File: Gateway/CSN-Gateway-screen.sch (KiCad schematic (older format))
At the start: 17 parts, among them IC2 FT232RL, P1 USB_MINI, P2 CONN_01X12, P4 CONN_OLED_SCREEN, SW1 SW_PUSH, SW2 SW_PUSH

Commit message: new pcb for v1.1 prototype
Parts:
- removed C2: 0.1uF, Capacitors_SMD:C_0805_HandSoldering, symbol C
- removed R20: 4k7, Resistors_SMD:R_0805_HandSoldering, symbol R
- removed R21: 10k, Resistors_SMD:R_0805_HandSoldering, symbol R
- added C1: 100nF, Capacitors_SMD:C_0805_HandSoldering, symbol C
- C19: value 100nF -> 10uF; footprint Capacitors_SMD:C_0805_HandSoldering -> Capacitors_Tantalum_SMD:CP_Tantalum_Case-R_EIA-2012-12_Hand; symbol C -> CP1
- P2: footprint Pin_Headers:Pin_Header_Straight_1x12 -> Connectors:IDC_Header_Straight_12pins
- R16, R22, R23: value 100 -> 1K
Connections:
- net GND: now also C1.1
- net RST: now also IC2.2 (!DTR)
- net VCC: no longer C15.1, C19.1, IC2.20 (VCC), IC2.4 (VCCIO)
- net at IC2.17 (3V3OUT): now also C1.2
- net at P1.1 (VCC): now also C15.1, C19.1, IC2.20 (VCC), IC2.4 (VCCIO)
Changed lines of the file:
@@
 P 5650 4050
 F 0 "R16" V 5730 4050 50  0000 C CNN
-F 1 "100" V 5650 4050 50  0000 C CNN
+F 1 "1K" V 5650 4050 50  0000 C CNN
 F 2 "Resistors_SMD:R_0805_HandSoldering" V 5580 4050 50  0001 C CNN
 F 3 "" H 5650 4050 50  0000 C CNN
@@
 NoConn ~ 7100 2300
 NoConn ~ 7100 2400
-NoConn ~ 5900 1700
-$Comp
-L C C2
-U 1 1 583B6E0E
-P 7450 1800
-F 0 "C2" H 7475 1900 50  0000 L CNN
-F 1 "0.1uF" H 7475 1700 50  0000 L CNN
-F 2 "Capacitors_SMD:C_0805_HandSoldering" H 7488 1650 50  0001 C CNN
-F 3 "" H 7450 1800 50  0000 C CNN
-	1    7450 1800
-	0    1    1    0
-$EndComp
-Text GLabel 7750 1800 2    60   Input ~ 0
+Text GLabel 7300 1800 2    60   Input ~ 0
 RST
 $Comp
@@
 	0    -1   1    0
 $EndComp
-$Comp
-L R R20
-U 1 1 583B4E04
-P 5200 2000
-F 0 "R20" V 5280 2000 50  0000 C CNN
-F 1 "4k7" V 5200 2000 50  0000 C CNN
-F 2 "Resistors_SMD:R_0805_HandSoldering" V 5130 2000 50  0001 C CNN
-F 3 "" H 5200 2000 50  0000 C CNN
-	1    5200 2000
-	1    0    0    -1
-$EndComp
-$Comp
-L R R21
-U 1 1 583B4EB8
-P 5200 2500
-F 0 "R21" V 5280 2500 50  0000 C CNN
-F 1 "10k" V 5200 2500 50  0000 C CNN
-F 2 "Resistors_SMD:R_0805_HandSoldering" V 5130 2500 50  0001 C CNN
-F 3 "" H 5200 2500 50  0000 C CNN
-	1    5200 2500
-	1    0    0    -1
-$EndComp
-$Comp
-L GND #PWR08
-U 1 1 583B546D
-P 5200 2800
-F 0 "#PWR08" H 5200 2550 50  0001 C CNN
-F 1 "GND" H 5200 2650 50  0000 C CNN
-F 2 "" H 5200 2800 50  0000 C CNN
-F 3 "" H 5200 2800 50  0000 C CNN
-	1    5200 2800
-	1    0    0    -1
-$EndComp
 NoConn ~ 4800 1900
 $Comp
@@
 P 5650 4250
 F 0 "R22" V 5730 4250 50  0000 C CNN
-F 1 "100" V 5650 4250 50  0000 C CNN
+F 1 "1K" V 5650 4250 50  0000 C CNN
 F 2 "Resistors_SMD:R_0805_HandSoldering" V 5580 4250 50  0001 C CNN
 F 3 "" H 5650 4250 50  0000 C CNN
@@
 P 5650 4450
 F 0 "R23" V 5730 4450 50  0000 C CNN
-F 1 "100" V 5650 4450 50  0000 C CNN
+F 1 "1K" V 5650 4450 50  0000 C CNN
 F 2 "Resistors_SMD:R_0805_HandSoldering" V 5580 4450 50  0001 C CNN
 F 3 "" H 5650 4450 50  0000 C CNN
@@
 $EndComp
 $Comp
-L GND #PWR09
+L GND #PWR08
 U 1 1 583CF5CF
 P 4700 1200
-F 0 "#PWR09" H 4700 950 50  0001 C CNN
+F 0 "#PWR08" H 4700 950 50  0001 C CNN
 F 1 "GND" H 4700 1050 50  0000 C CNN
 F 2 "" H 4700 1200 50  0000 C CNN
@@
 $EndComp
 $Comp
-L GND #PWR010
+L GND #PWR09
 U 1 1 583D70C6
 P 8250 5200
-F 0 "#PWR010" H 8250 4950 50  0001 C CNN
+F 0 "#PWR09" H 8250 4950 50  0001 C CNN
 F 1 "GND" H 8250 5050 50  0000 C CNN
 F 2 "" H 8250 5200 50  0000 C CNN
@@
 $EndComp
 $Comp
-L VCC #PWR011
+L VCC #PWR010
 U 1 1 583D70CC
 P 8250 4100
-F 0 "#PWR011" H 8250 3950 50  0001 C CNN
+F 0 "#PWR010" H 8250 3950 50  0001 C CNN
 F 1 "VCC" H 8250 4250 50  0000 C CNN
 F 2 "" H 8250 4100 50  0000 C CNN
@@
 BTN2
 $Comp
-L C C19
+L CP1 C19
 U 1 1 583E37A8
 P 5050 1150
 F 0 "C19" V 5100 1200 50  0000 L CNN
-F 1 "100nF" V 5000 850 50  0000 L CNN
-F 2 "Capacitors_SMD:C_0805_HandSoldering" H 5088 1000 50  0001 C CNN
+F 1 "10uF" V 5000 850 50  0000 L CNN
+F 2 "Capacitors_Tantalum_SMD:CP_Tantalum_Case-R_EIA-2012-12_Hand" H 5088 1000 50  0001 C CNN
 F 3 "" H 5050 1150 50  0000 C CNN
 	1    5050 1150
 	0    1    1    0
-$EndComp
-$Comp
-L VCC #PWR012
-U 1 1 583E4A2E
-P 5750 900
-F 0 "#PWR012" H 5750 750 50  0001 C CNN
-F 1 "VCC" H 5750 1050 50  0000 C CNN
-F 2 "" H 5750 900 50  0000 C CNN
-F 3 "" H 5750 900 50  0000 C CNN
-	1    5750 900
-	1    0    0    -1
 $EndComp
 Text GLabel 5350 4050 0    60   Input ~ 0
@@
 F 0 "P2" H 2550 4350 50  0000 C CNN
 F 1 "CONN_01X12" V 2650 3700 50  0000 C CNN
-F 2 "Pin_Headers:Pin_Header_Straight_1x12" H 2550 3700 50  0000 C CNN
+F 2 "Connectors:IDC_Header_Straight_12pins" H 2550 3700 50  0001 C CNN
 F 3 "" H 2550 3700 50  0000 C CNN
 	1    2550 3700
@@
 $EndComp
 $Comp
-L GND #PWR013
+L GND #PWR011
 U 1 1 58405E61
 P 3700 3450
-F 0 "#PWR013" H 3700 3200 50  0001 C CNN
+F 0 "#PWR011" H 3700 3200 50  0001 C CNN
 F 1 "GND" H 3700 3300 50  0000 C CNN
 F 2 "" H 3700 3450 50  0000 C CNN
@@
 $EndComp
 $Comp
-L VCC #PWR014
+L VCC #PWR012
 U 1 1 58405E9F
 P 3700 2950
-F 0 "#PWR014" H 3700 2800 50  0001 C CNN
+F 0 "#PWR012" H 3700 2800 50  0001 C CNN
 F 1 "VCC" H 3700 3100 50  0000 C CNN
 F 2 "" H 3700 2950 50  0000 C CNN
@@
 	7100 1800 7300 1800
 Wire Wire Line
-	7600 1800 7750 1800
-Wire Wire Line
 	5900 2400 5750 2400
 Wire Wire Line
@@
 Connection ~ 5750 2700
 Wire Wire Line
-	5200 2150 5200 2350
-Wire Wire Line
-	5200 2650 5200 2800
-Wire Wire Line
-	4800 1700 4950 1700
-Wire Wire Line
-	4950 1700 4950 1300
-Wire Wire Line
-	4950 1300 5900 1300
-Wire Wire Line
-	4800 1800 5000 1800
-Wire Wire Line
-	5000 1800 5000 1400
-Wire Wire Line
-	5000 1400 5900 1400
+	4800 1700 5550 1700
+Wire Wire Line
+	5550 1700 5550 1300
+Wire Wire Line
+	5550 1300 5900 1300
+Wire Wire Line
+	4800 1800 5600 1800
+Wire Wire Line
+	5600 1800 5600 1400
+Wire Wire Line
+	5600 1400 5900 1400
 Wire Wire Line
 	9150 5200 9150 5150
@@
 	5800 4450 5850 4450
 Wire Wire Line
-	5200 1600 5200 1850
-Wire Wire Line
-	5200 2300 5500 2300
-Wire Wire Line
-	5500 2300 5500 2200
-Wire Wire Line
-	5500 2200 5900 2200
-Connection ~ 5200 2300
-Wire Wire Line
 	6550 4100 6550 4250
 Wire Wire Line
@@
 Connection ~ 4400 2200
 Wire Wire Line
-	4800 1600 5200 1600
+	5400 1600 4800 1600
 Wire Wire Line
 	4900 1150 4700 1150
@@
 Connection ~ 4700 1150
 Wire Wire Line
-	5200 1150 5750 1150
-Wire Wire Line
-	5750 900  5750 1800
-Wire Wire Line
 	5750 1600 5900 1600
 Wire Wire Line
 	5750 1800 5900 1800
 Connection ~ 5750 1600
-Connection ~ 5750 1150
 Wire Wire Line
 	5200 900  5400 900
 Wire Wire Line
-	5400 900  5400 1150
+	5400 900  5400 1600
 Connection ~ 5400 1150
 Wire Wire Line
@@
 	2750 4250 2850 4250
 $Comp
-L PWR_FLAG #FLG015
+L PWR_FLAG #FLG013
 U 1 1 5840701E
 P 3350 2950
-F 0 "#FLG015" H 3350 3045 50  0001 C CNN
+F 0 "#FLG013" H 3350 3045 50  0001 C CNN
 F 1 "PWR_FLAG" H 3350 3130 50  0000 C CNN
 F 2 "" H 3350 2950 50  0000 C CNN
@@
 $EndComp
 $Comp
-L PWR_FLAG #FLG016
+L PWR_FLAG #FLG014
 U 1 1 584070FC
 P 3350 3500
-F 0 "#FLG016" H 3350 3595 50  0001 C CNN
+F 0 "#FLG014" H 3350 3595 50  0001 C CNN
 F 1 "PWR_FLAG" H 3350 3680 50  0000 C CNN
 F 2 "" H 3350 3500 50  0000 C CNN
@@
 Wire Wire Line
 	9050 2350 8950 2350
+$Comp
+L C C1
+U 1 1 58AC3203
+P 5400 2500
+F 0 "C1" V 5450 2550 50  0000 L CNN
+F 1 "100nF" V 5450 2200 50  0000 L CNN
+F 2 "Capacitors_SMD:C_0805_HandSoldering" H 5438 2350 50  0001 C CNN
+F 3 "" H 5400 2500 50  0000 C CNN
+	1    5400 2500
+	-1   0    0    1
+$EndComp
+$Comp
+L GND #PWR015
+U 1 1 58AC332D
+P 5400 2800
+F 0 "#PWR015" H 5400 2550 50  0001 C CNN
+F 1 "GND" H 5400 2650 50  0000 C CNN
+F 2 "" H 5400 2800 50  0000 C CNN
+F 3 "" H 5400 2800 50  0000 C CNN
+	1    5400 2800
+	1    0    0    -1
+$EndComp
+Wire Wire Line
+	5400 2650 5400 2800
+NoConn ~ 5900 2200
+Wire Wire Line
+	5900 1700 5700 1700
+Wire Wire Line
+	5700 1700 5700 2150
+Wire Wire Line
+	5700 2150 5400 2150
+Wire Wire Line
+	5400 2150 5400 2350
+Wire Wire Line
+	5200 1150 5750 1150
+Wire Wire Line
+	5750 1150 5750 1800
 $EndSCHEMATC

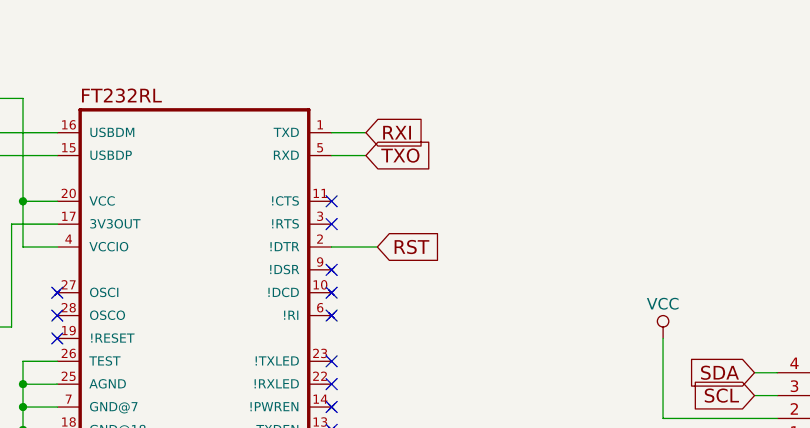
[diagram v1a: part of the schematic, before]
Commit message: Fix wrong reset pin for ICSP, fix exchange of rx/tx in ftdi
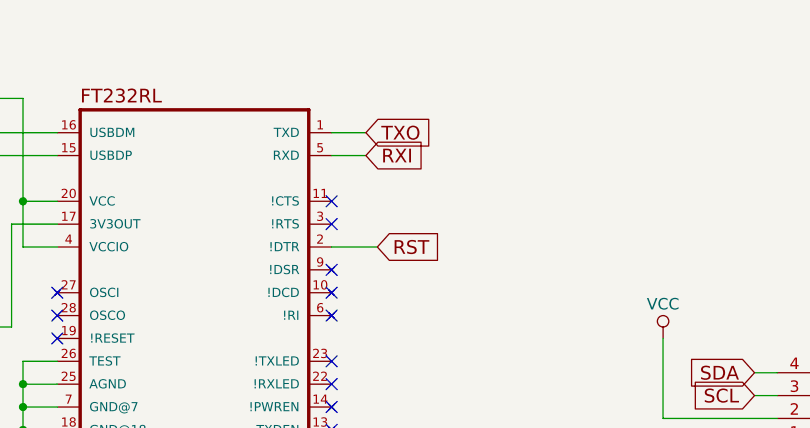
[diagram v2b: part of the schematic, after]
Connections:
- net RXI: now also IC2.5 (RXD); no longer IC2.1 (TXD)
- net TXO: now also IC2.1 (TXD); no longer IC2.5 (RXD)
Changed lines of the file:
@@
 $EndComp
 Text GLabel 7250 1300 2    60   Input ~ 0
+TXO
+Text GLabel 7250 1400 2    60   Input ~ 0
 RXI
-Text GLabel 7250 1400 2    60   Input ~ 0
-TXO
 NoConn ~ 5900 2000
 NoConn ~ 5900 2100

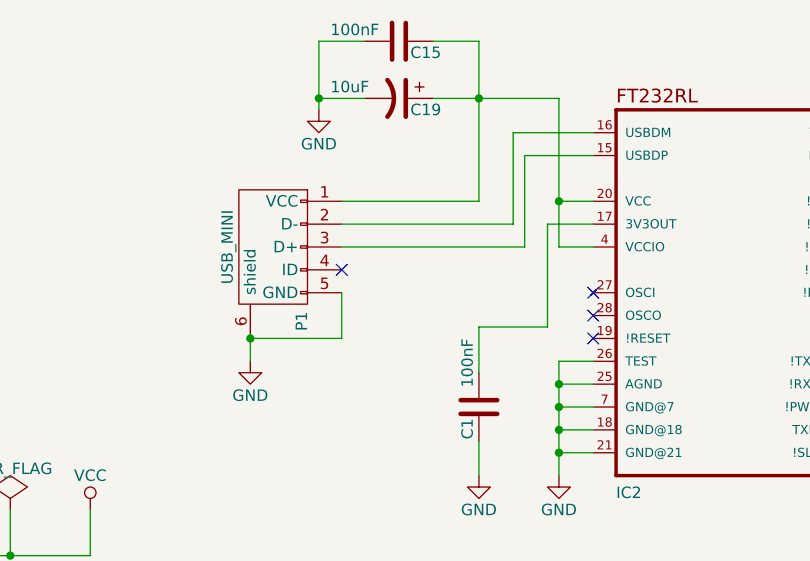
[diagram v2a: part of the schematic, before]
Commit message: add BOM
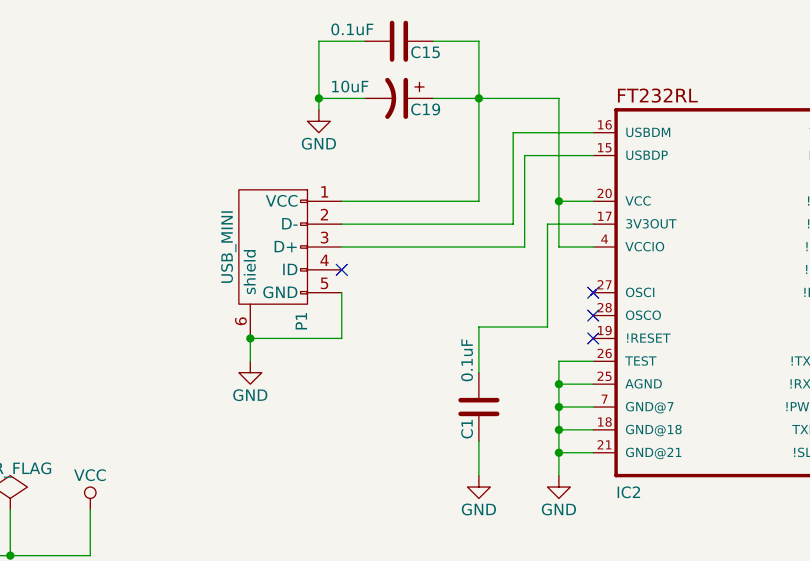
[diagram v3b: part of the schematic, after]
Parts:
- C1, C15: value 100nF -> 0.1uF
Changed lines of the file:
@@
 P 5050 900
 F 0 "C15" V 5100 950 50  0000 L CNN
-F 1 "100nF" V 5000 600 50  0000 L CNN
+F 1 "0.1uF" V 5000 600 50  0000 L CNN
 F 2 "Capacitors_SMD:C_0805_HandSoldering" H 5088 750 50  0001 C CNN
 F 3 "" H 5050 900 50  0000 C CNN
@@
 P 5400 2500
 F 0 "C1" V 5450 2550 50  0000 L CNN
-F 1 "100nF" V 5450 2200 50  0000 L CNN
+F 1 "0.1uF" V 5450 2200 50  0000 L CNN
 F 2 "Capacitors_SMD:C_0805_HandSoldering" H 5438 2350 50  0001 C CNN
 F 3 "" H 5400 2500 50  0000 C CNN
